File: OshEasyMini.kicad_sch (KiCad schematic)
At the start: 121 parts, among them J1 TAGCONNECT, J10 Conn_01x04_MountingPin, J3 SMA_Edgelaunch, J4 Screw_Terminal_01x03, J5 UFL, J6 Conn_01x02, Q1 SiA449DJ, Q2 AO3400A, Q3 SiA449DJ, U1 MIA-M10Q, U11 CPT-7502-65-SMT-TR, U12 LM293QT, U17 MCP73831-2-OT, U18 TC2185-3.3VxCTTR, U19 W25Q64JVXGIQ, U2 WE-TVS-82400102, U20 SISB46DN, U21 SN74LVC1G80QDCKTQ1, U3 ADXL375, U4 MS5607-02BA, U6 MCP130-xxxxTT, U7 DRV5012AEDMRR, U8 CC1200, U9 ATSAMD21G17D-A, X2 ECS-160-8-36Q-AES-TR1, Y1 40mhz 8pF 30 Ohms, Y2 32.768khz

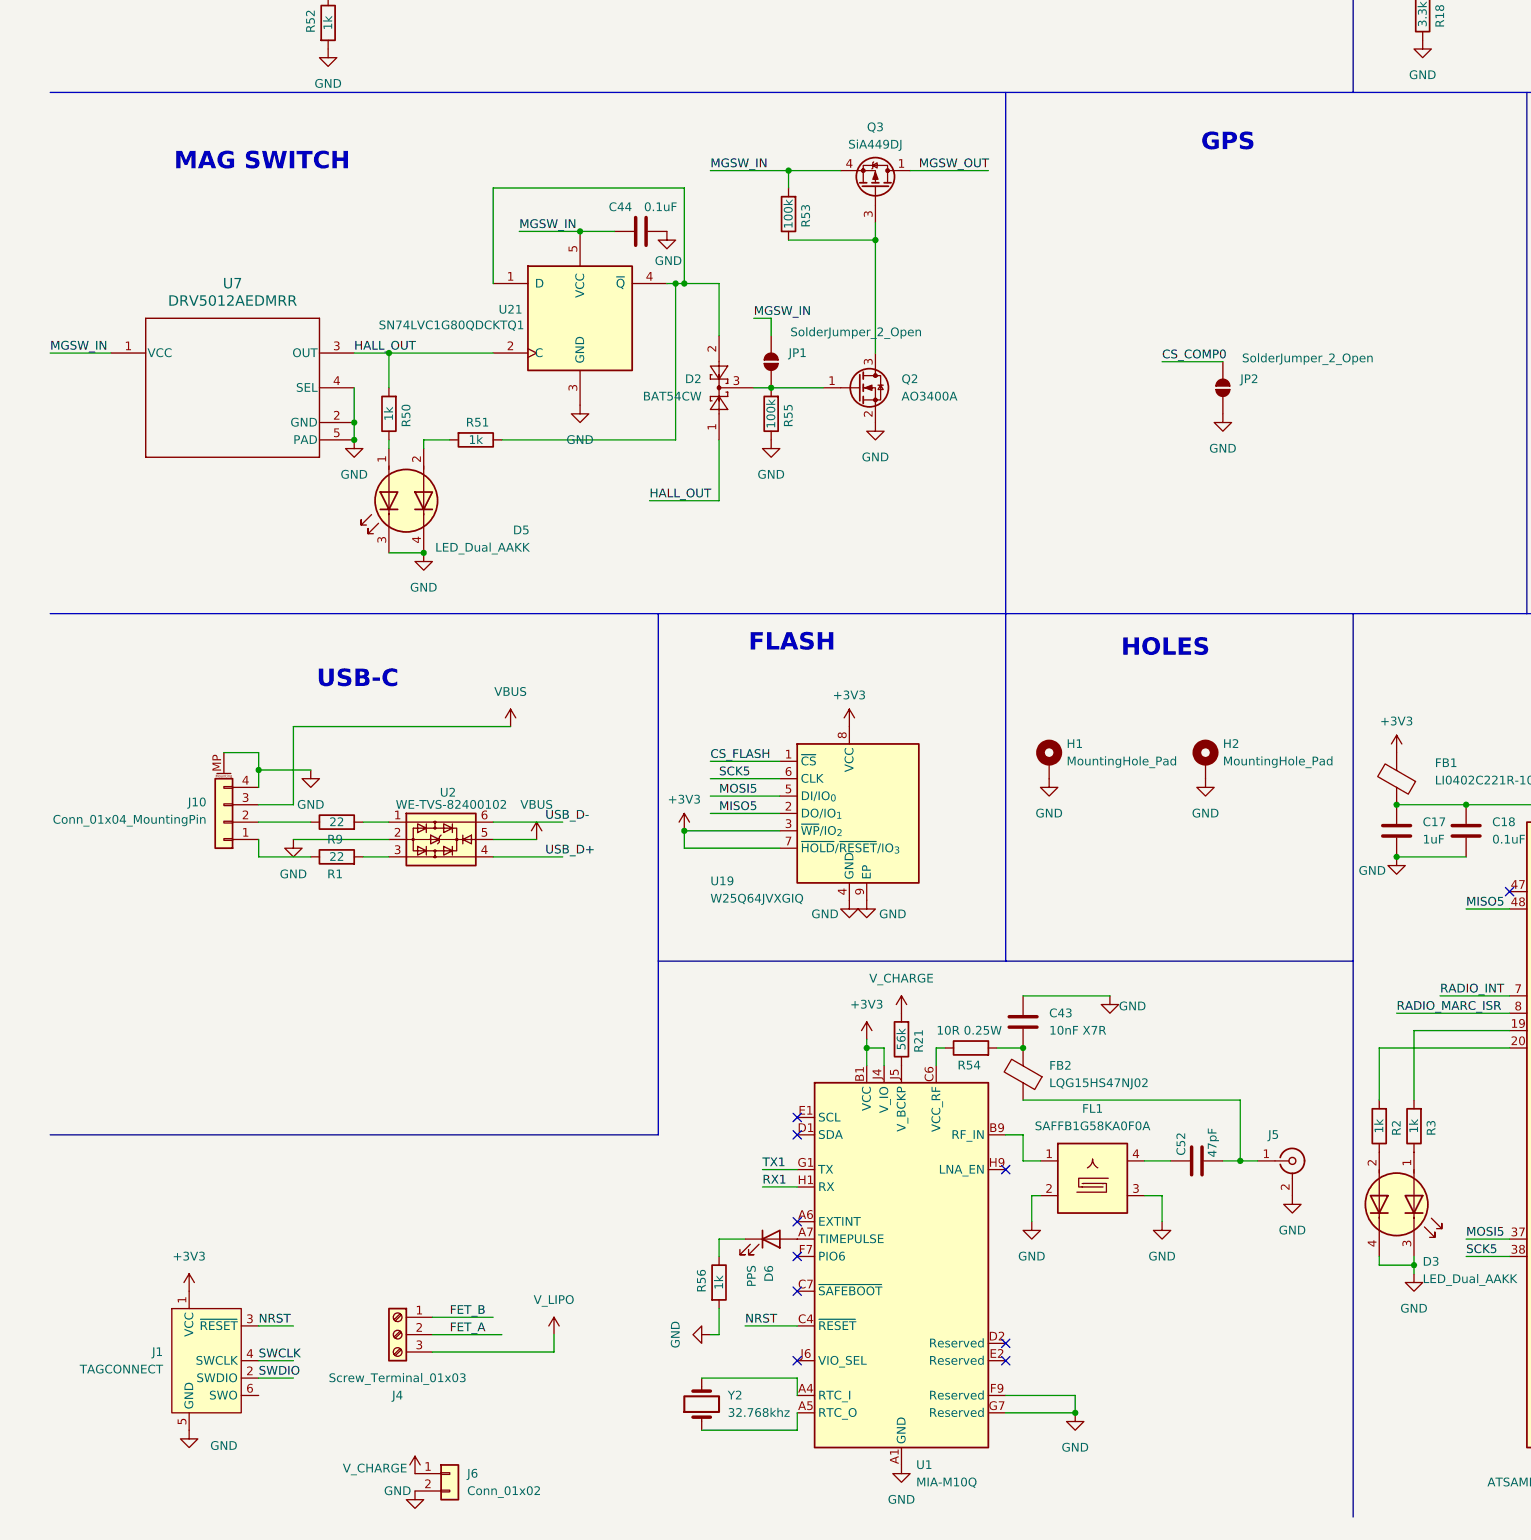
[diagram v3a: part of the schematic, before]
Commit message: finished usbc daughterboard, next removing charging circuitry onboard
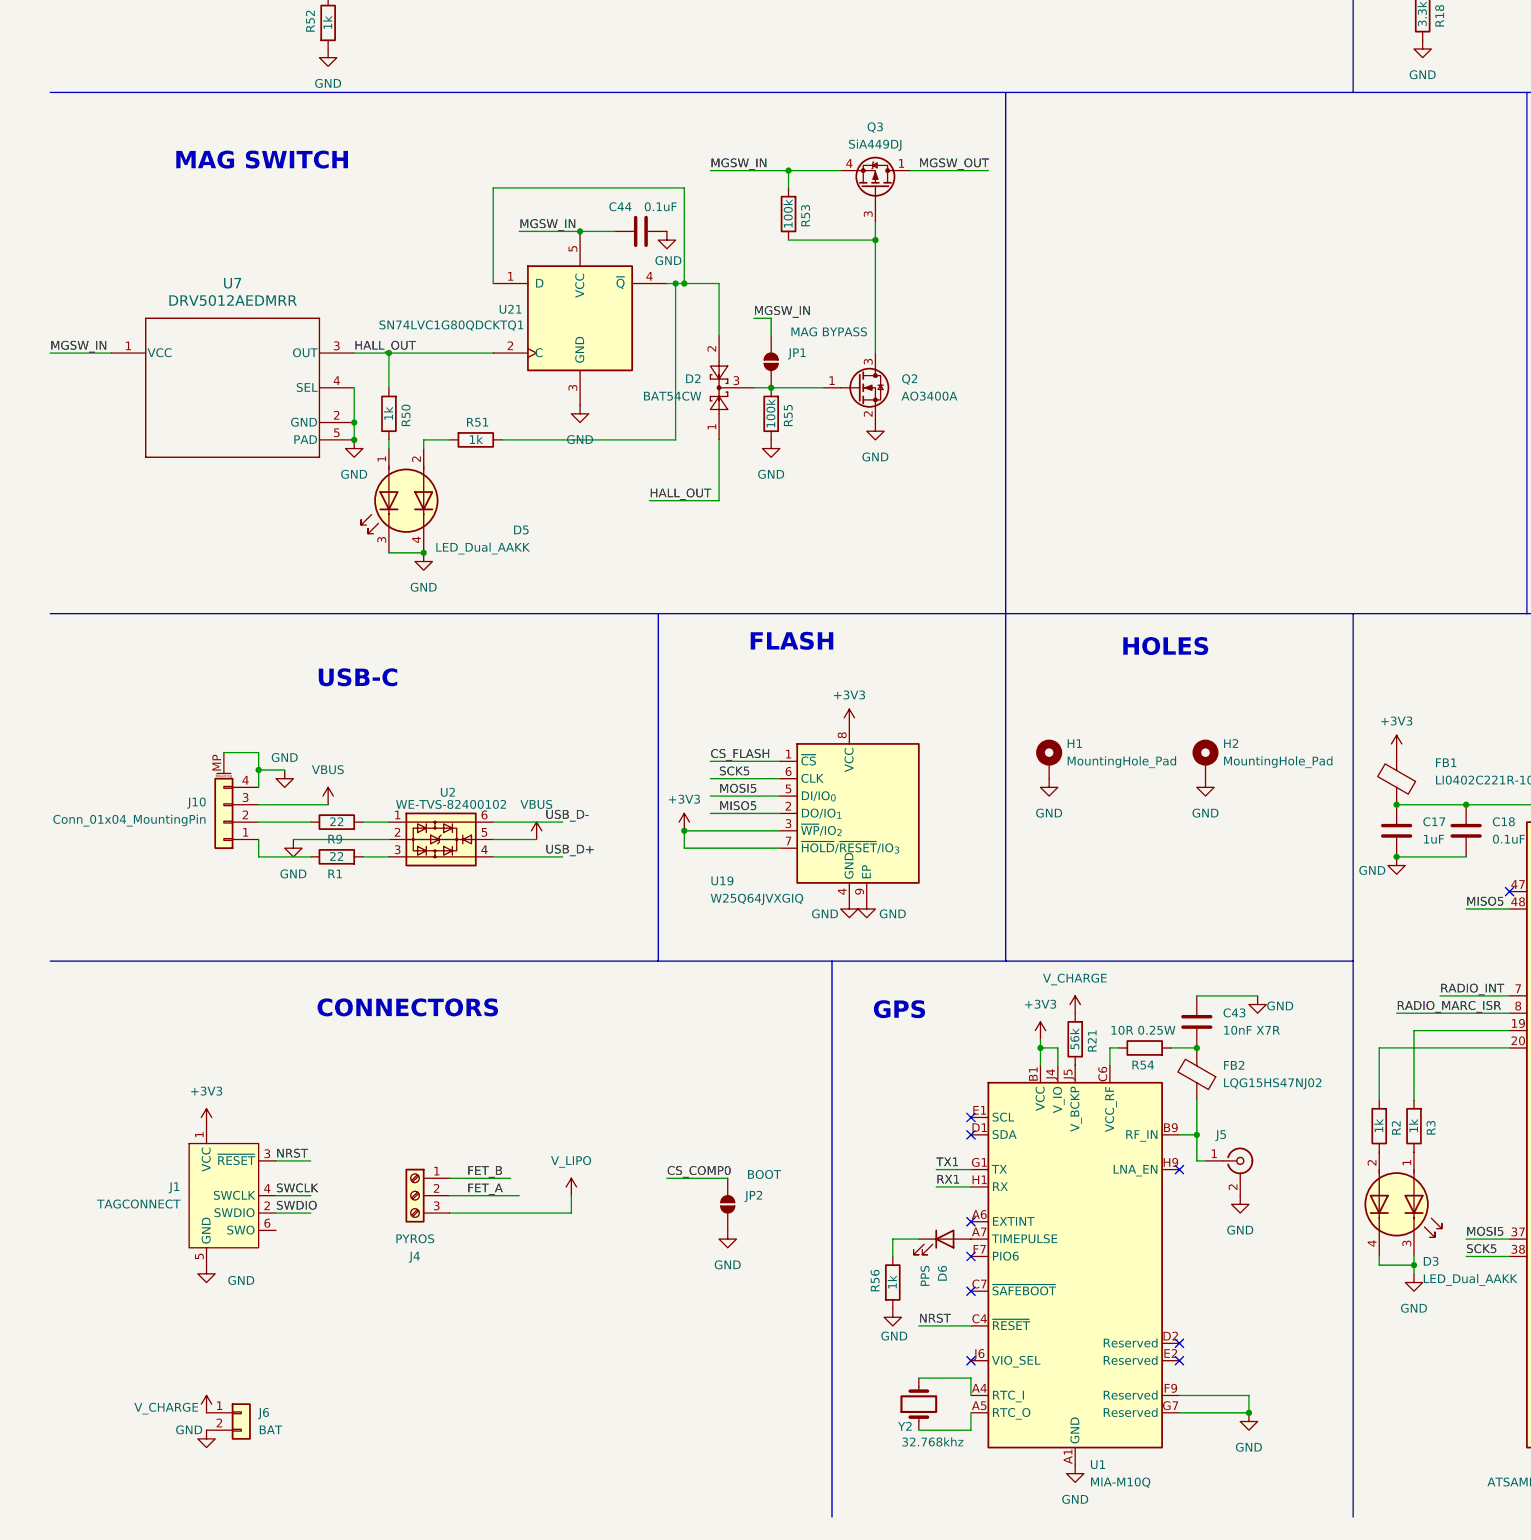
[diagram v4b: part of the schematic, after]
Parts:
- removed C52: 47pF, Capacitor_SMD:C_0402_1005Metric, symbol Device:C
- removed FL1: SAFFB1G58KA0F0A, Filter:Filter_1109-5_1.1x0.9mm, symbol Filter:SAFFB1G58KA0F0A
- J4: value Screw_Terminal_01x03 -> PYROS
- J6: value Conn_01x02 -> BAT
- JP1: value SolderJumper_2_Open -> MAG BYPASS
- JP2: value SolderJumper_2_Open -> BOOT
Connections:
- net at FB2.1, J5.1 (In): now also U1.B9 (RF_IN)
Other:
- note added: "CONNECTORS"
- moved on the sheet: C43, D6, FB2, J1, J4, J5, J6, JP2, R21, R54, R56, U1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

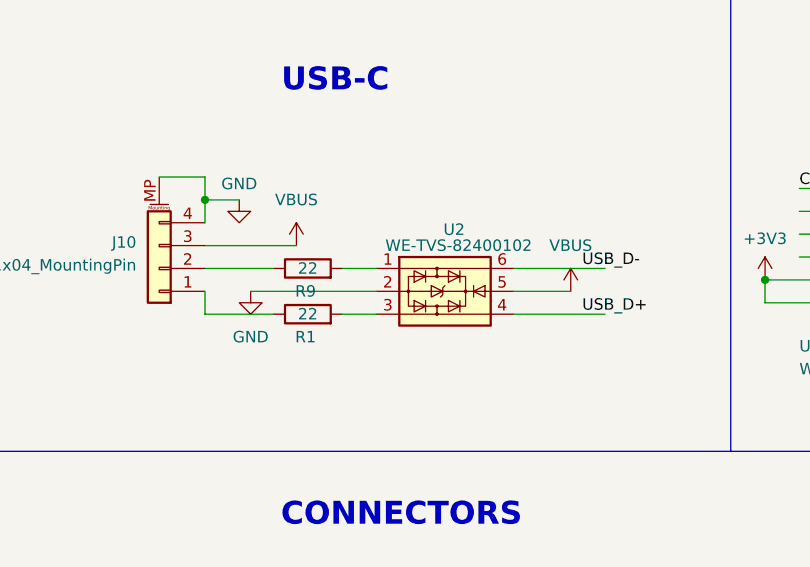
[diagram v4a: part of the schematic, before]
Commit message: ready for final prod after silkscreens
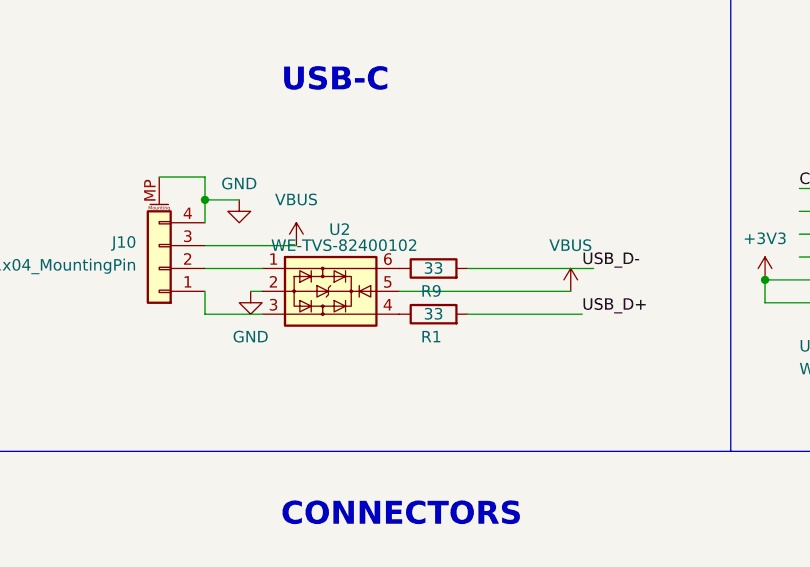
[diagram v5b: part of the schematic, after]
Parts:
- R1, R9: value 22 -> 33
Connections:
- net USB_D+: now also R1.2; no longer U2.4
- net USB_D-: now also R9.2; no longer U2.6
- net at U2.1: now also J10.2 (Pin_2); no longer R9.2
- net at U2.3: now also J10.1 (Pin_1); no longer R1.2
- net at R9.1: now also U2.6; no longer J10.2 (Pin_2)
- net at R1.1: now also U2.4; no longer J10.1 (Pin_1)
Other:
- company: (none) -> Leviathan Flight Systems
- title: (none) -> MetrumITX
- moved on the sheet: R1, R9, U2
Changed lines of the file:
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@@
 	(generator_version "9.0")
 	(paper "A3")
+	(title_block
+		(title "MetrumITX")
+		(date "2025-12-19")
+		(rev "v1.0")
+		(company "Leviathan Flight Systems")
+	)
 	(text "FLASH"
 		(exclude_from_sim no)
@@
 	(wire
 		(pts
-			(xy 50.8 187.96) (xy 43.18 187.96)
+			(xy 43.18 187.96) (xy 49.53 187.96)
 		)
 		(stroke
@@
 	(wire
 		(pts
-			(xy 43.18 182.88) (xy 50.8 182.88)
+			(xy 43.18 182.88) (xy 49.53 182.88)
+		)
+		(stroke
+			(width 0)
+			(type default)
+		)
+	)
+	(wire
+		(pts
+			(xy 72.39 182.88) (xy 86.36 182.88)
 		)
 		(stroke
@@
 	(wire
 		(pts
-			(xy 77.47 182.88) (xy 87.63 182.88)
-		)
-		(stroke
-			(width 0)
-			(type default)
-		)
-	)
-	(wire
-		(pts
 			(xy 120.65 45.72) (xy 133.35 45.72)
 		)
@@
 	(wire
 		(pts
-			(xy 77.47 187.96) (xy 87.63 187.96)
-		)
-		(stroke
-			(width 0)
-			(type default)
-		)
-	)
-	(wire
-		(pts
 			(xy 368.3 88.9) (xy 368.3 91.44)
 		)
@@
 	(wire
 		(pts
-			(xy 58.42 182.88) (xy 62.23 182.88)
-		)
-		(stroke
-			(width 0)
-			(type default)
-		)
-	)
-	(wire
-		(pts
 			(xy 237.49 116.84) (xy 247.65 116.84)
 		)
@@
 	(wire
 		(pts
+			(xy 72.39 187.96) (xy 85.09 187.96)
+		)
+		(stroke
+			(width 0)
+			(type default)
+		)
+	)
+	(wire
+		(pts
 			(xy 53.34 43.18) (xy 48.26 43.18)
 		)
@@
 	(wire
 		(pts
-			(xy 77.47 185.42) (xy 83.82 185.42)
+			(xy 64.77 185.42) (xy 83.82 185.42)
 		)
 		(stroke
@@
 	(wire
 		(pts
-			(xy 62.23 185.42) (xy 48.26 185.42)
+			(xy 49.53 185.42) (xy 48.26 185.42)
 		)
 		(stroke
@@
 	(wire
 		(pts
-			(xy 58.42 187.96) (xy 62.23 187.96)
-		)
-		(stroke
-			(width 0)
-			(type default)
-		)
-	)
-	(wire
-		(pts
 			(xy 325.12 227.33) (xy 326.39 227.33)
 		)
@@
 	(symbol
 		(lib_id "Power_Protection:WE-TVS-82400102")
-		(at 69.85 185.42 0)
+		(at 57.15 185.42 0)
 		(unit 1)
 		(exclude_from_sim no)
@@
 		(dnp no)
 		(property "Reference" "U2"
-			(at 70.866 178.562 0)
+			(at 58.166 178.562 0)
 			(effects
 				(font
@@
 		)
 		(property "Value" "WE-TVS-82400102"
-			(at 71.374 180.34 0)
+			(at 58.674 180.34 0)
 			(effects
 				(font
@@
 		)
 		(property "Footprint" "Package_TO_SOT_SMD:SOT-23-6"
-			(at 69.85 190.5 0)
+			(at 57.15 190.5 0)
 			(effects
 				(font
@@
 		)
 		(property "Datasheet" "https://www.we-online.com/components/products/datasheet/82400102.pdf"
-			(at 69.85 191.77 0)
+			(at 57.15 191.77 0)
 			(effects
 				(font
@@
 		)
 		(property "Description" "Low Capacitance TVS Diode Array, 2 Channels, SOT-23-6"
-			(at 69.85 185.42 0)
+			(at 57.15 185.42 0)
 			(effects
 				(font
@@
 	(symbol
 		(lib_id "Device:R")
-		(at 54.61 182.88 90)
+		(at 68.58 182.88 90)
 		(unit 1)
 		(exclude_from_sim no)
@@
 		(dnp no)
 		(property "Reference" "R9"
-			(at 54.356 185.42 90)
+			(at 68.326 185.42 90)
 			(effects
 				(font
@@
 			)
 		)
-		(property "Value" "22"
-			(at 54.61 182.88 90)
+		(property "Value" "33"
+			(at 68.58 182.88 90)
 			(effects
 				(font
@@
 		)
 		(property "Footprint" "Resistor_SMD:R_0201_0603Metric"
-			(at 54.61 184.658 90)
+			(at 68.58 184.658 90)
 			(effects
 				(font
@@
 		)
 		(property "Datasheet" "~"
-			(at 54.61 182.88 0)
+			(at 68.58 182.88 0)
 			(effects
 				(font
@@
 		)
 		(property "Description" "Resistor"
-			(at 54.61 182.88 0)
+			(at 68.58 182.88 0)
 			(effects
 				(font
@@
 	(symbol
 		(lib_id "Device:R")
-		(at 54.61 187.96 90)
+		(at 68.58 187.96 90)
 		(unit 1)
 		(exclude_from_sim no)
@@
 		(dnp no)
 		(property "Reference" "R1"
-			(at 54.356 190.5 90)
+			(at 68.326 190.5 90)
 			(effects
 				(font
@@
 			)
 		)
-		(property "Value" "22"
-			(at 54.61 187.96 90)
+		(property "Value" "33"
+			(at 68.58 187.96 90)
 			(effects
 				(font
@@
 		)
 		(property "Footprint" "Resistor_SMD:R_0201_0603Metric"
-			(at 54.61 189.738 90)
+			(at 68.58 189.738 90)
 			(effects
 				(font
@@
 		)
 		(property "Datasheet" "~"
-			(at 54.61 187.96 0)
+			(at 68.58 187.96 0)
 			(effects
 				(font
@@
 		)
 		(property "Description" "Resistor"
-			(at 54.61 187.96 0)
+			(at 68.58 187.96 0)
 			(effects
 				(font
